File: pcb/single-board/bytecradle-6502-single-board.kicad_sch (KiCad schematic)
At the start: 28 parts, among them J1 USB_B, SW1 SW_SPDT, SW2 RESET, SW3 NMI, U1 74AC14, U2 W65C02, U3 CD74HC688, U4 74AC08, X1 14 MHz

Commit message: Routing
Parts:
- H1, H2, H3, H4: footprint MountingHole:MountingHole_3.2mm_M3 -> MountingHole:MountingHole_3.2mm_M3_DIN965_Pad_TopOnly
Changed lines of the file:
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@@
 			)
 		)
-		(property "Footprint" "MountingHole:MountingHole_3.2mm_M3"
+		(property "Footprint" "MountingHole:MountingHole_3.2mm_M3_DIN965_Pad_TopOnly"
 			(at 260.35 124.46 0)
 			(effects
@@
 			)
 		)
-		(property "Footprint" "MountingHole:MountingHole_3.2mm_M3"
+		(property "Footprint" "MountingHole:MountingHole_3.2mm_M3_DIN965_Pad_TopOnly"
 			(at 260.35 118.11 0)
 			(effects
@@
 			)
 		)
-		(property "Footprint" "MountingHole:MountingHole_3.2mm_M3"
+		(property "Footprint" "MountingHole:MountingHole_3.2mm_M3_DIN965_Pad_TopOnly"
 			(at 260.35 137.16 0)
 			(effects
@@
 			)
 		)
-		(property "Footprint" "MountingHole:MountingHole_3.2mm_M3"
+		(property "Footprint" "MountingHole:MountingHole_3.2mm_M3_DIN965_Pad_TopOnly"
 			(at 260.35 130.81 0)
 			(effects

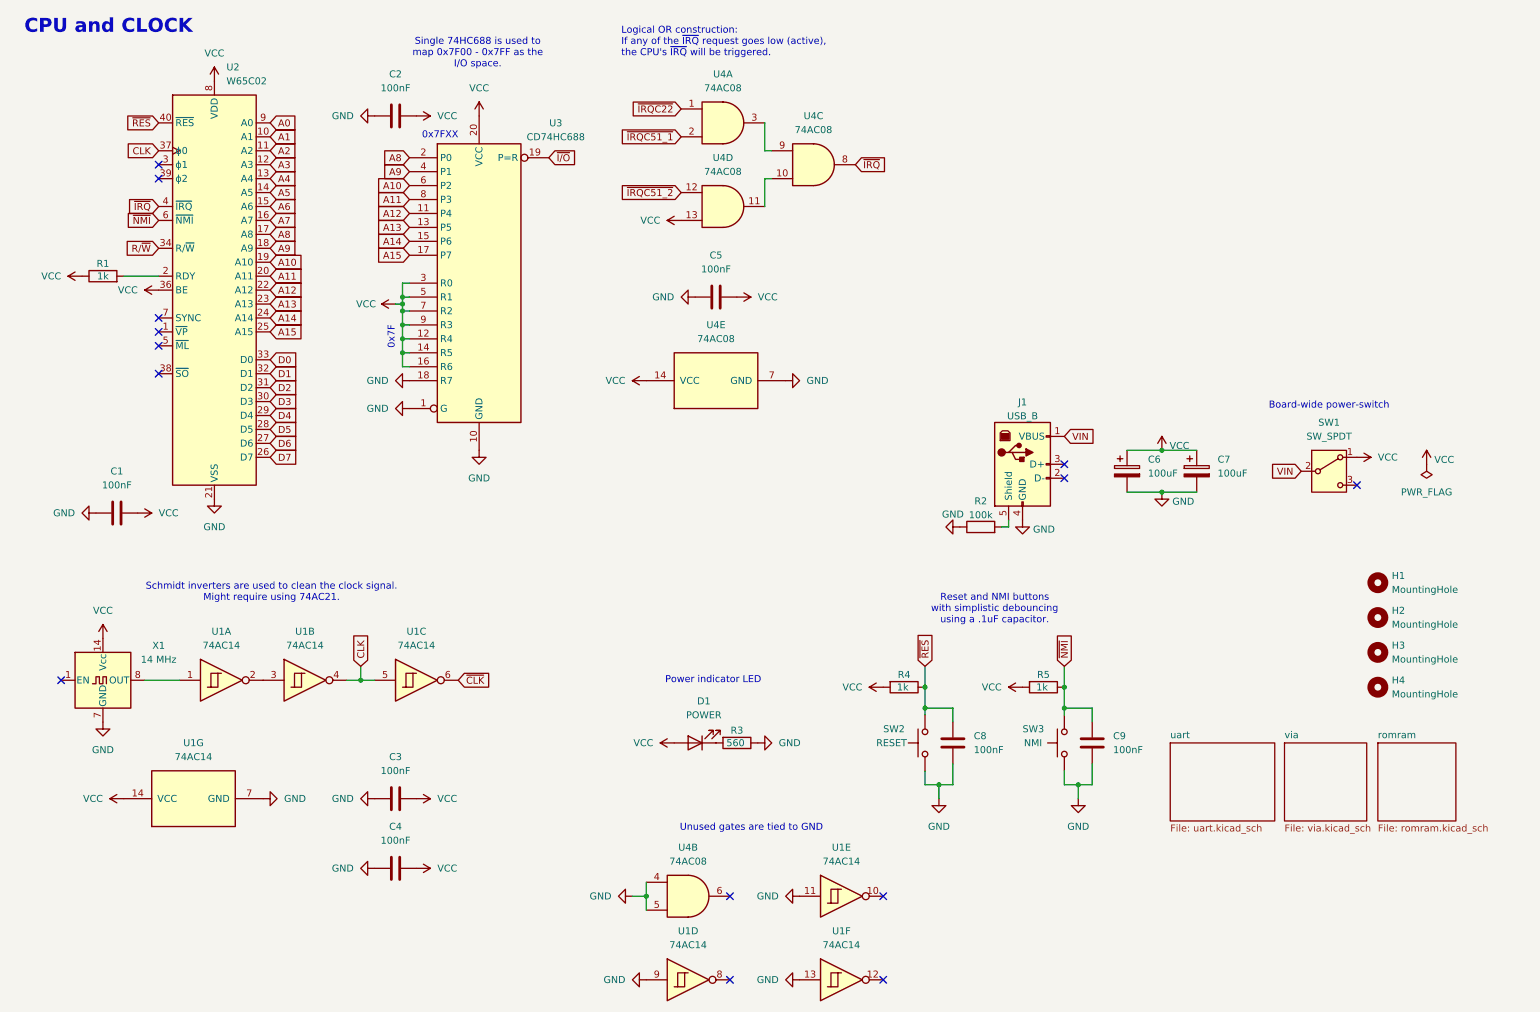
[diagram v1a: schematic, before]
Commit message: Initial commit bitbang SD-card routines
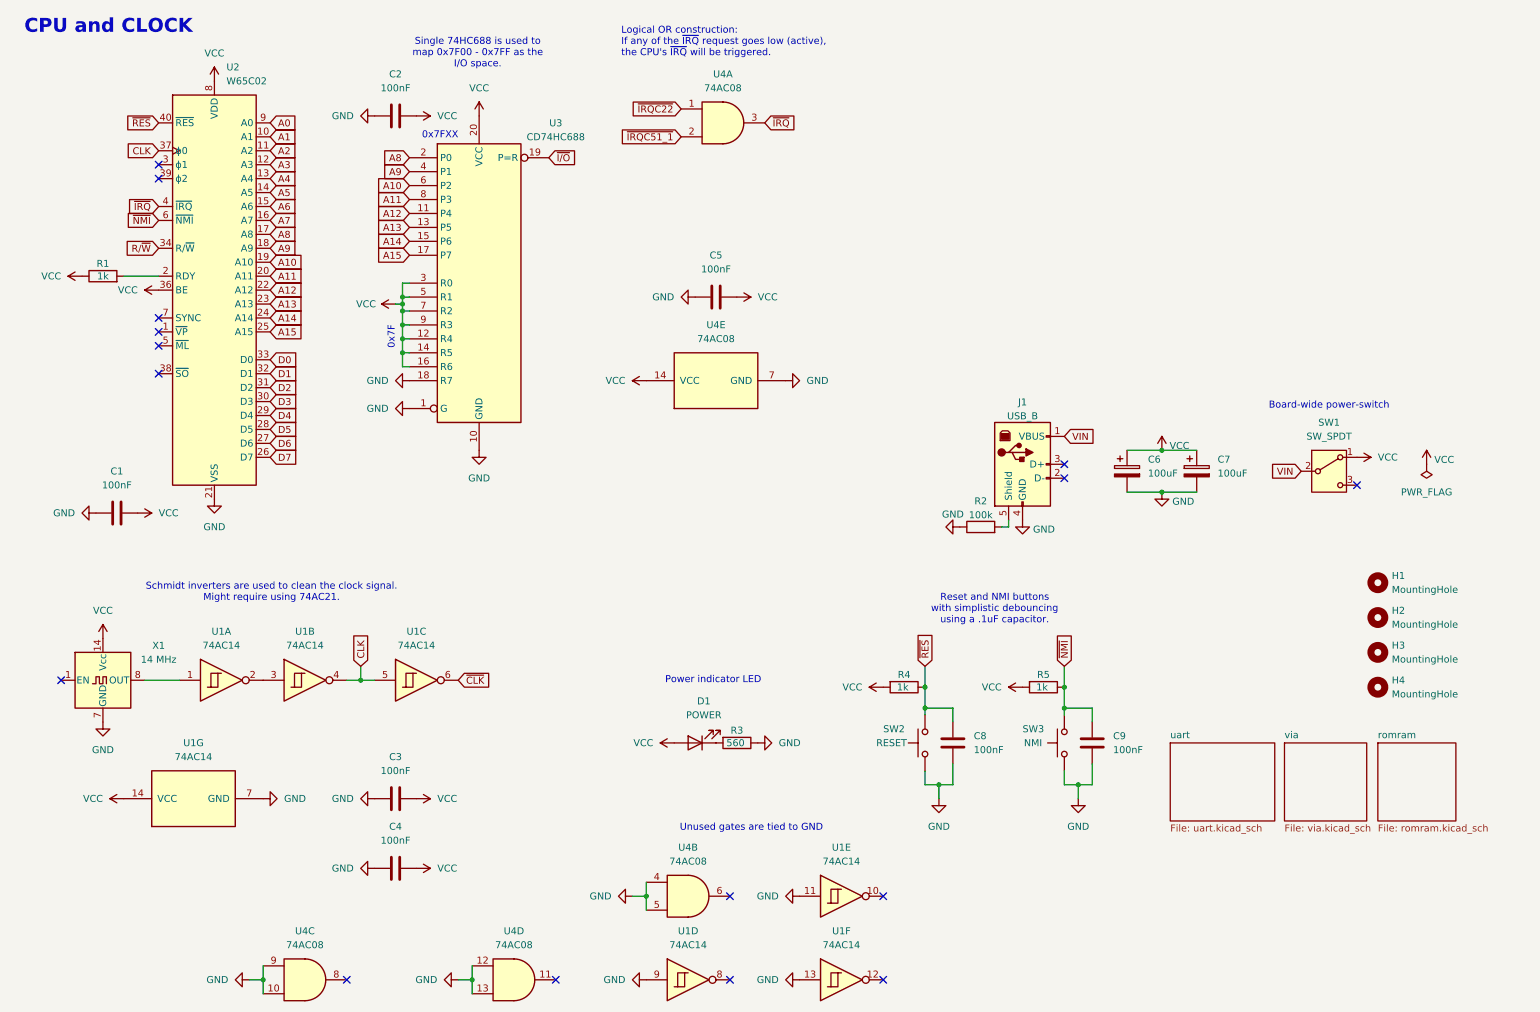
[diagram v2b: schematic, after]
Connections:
- net ~{IRQC51_2} is gone; now on net GND: U4.12
- net GND: now also U4.10, U4.13, U4.9
- net VCC: no longer U4.13
- net ~{IRQ}: now also U4.3; no longer U4.8
- net at U4.11: no longer U4.10
- no-connect marks 14 -> 16
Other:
- moved on the sheet: U4C, U4D

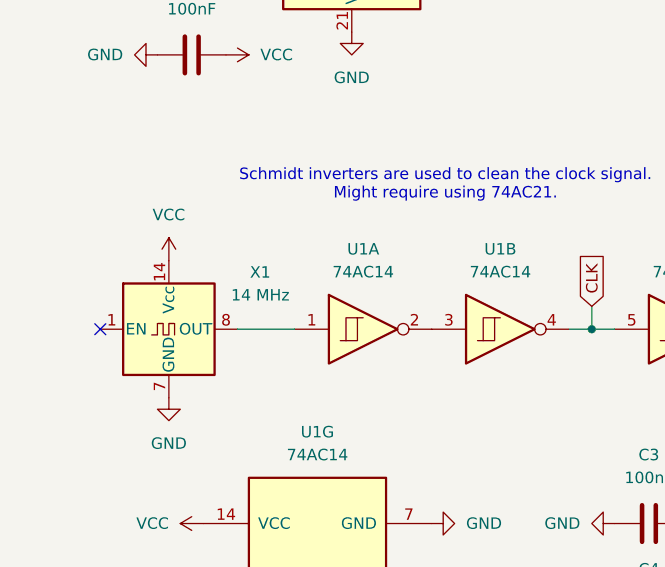
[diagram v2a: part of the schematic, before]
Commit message: Cleaning repository and completing SD-card reading using bitbang SPI
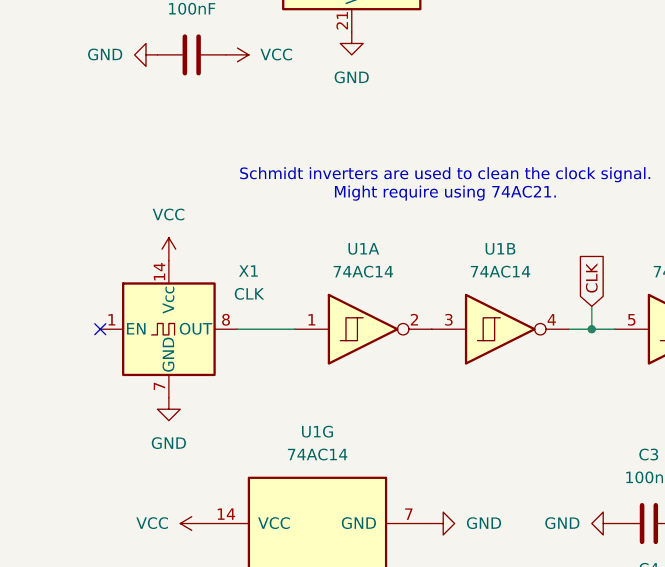
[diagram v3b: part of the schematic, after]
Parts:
- X1: value 14 MHz -> CLK
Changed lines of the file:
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@@
 		(fields_autoplaced yes)
 		(property "Reference" "X1"
-			(at 38.1 129.5714 0)
+			(at 36.83 129.4698 0)
 			(effects
 				(font
@@
 			)
 		)
-		(property "Value" "14 MHz"
-			(at 38.1 132.1114 0)
+		(property "Value" "CLK"
+			(at 36.83 132.0098 0)
 			(effects
 				(font
